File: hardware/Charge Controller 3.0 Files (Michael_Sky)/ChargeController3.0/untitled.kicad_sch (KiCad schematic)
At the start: 3 parts, among them J1 Conn_02x26_Odd_Even, J12 Conn_02x26_Odd_Even, J20 Conn_01x08_Pin

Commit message: fixed merge :(
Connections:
- net 3.3V: now also J12.28 (Pin_28)
- net GND: now also J1.33 (Pin_33), J1.34 (Pin_34), J12.29 (Pin_29), J20.3 (Pin_3), J20.4 (Pin_4)
- net RS SYS2 Tx: now also J1.40 (Pin_40)
- net SYS/BATT: now also J20.1 (Pin_1), J20.2 (Pin_2)
- net UART_RX: now also J1.42 (Pin_42)
- net UART_TX: now also J1.44 (Pin_44)

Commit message: New formatting
New formatting
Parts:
- J20: footprint (none) -> Connector_PinHeader_2.54mm:PinHeader_1x08_P2.54mm_Horizontal
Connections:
- net INT: now also J1.12 (Pin_12); no longer J1.9 (Pin_9)
- net PG: now also J1.10 (Pin_10); no longer J1.18 (Pin_18)
- net SCL: now also J1.18 (Pin_18); no longer J1.10 (Pin_10)
- net SDA: now also J1.16 (Pin_16); no longer J1.12 (Pin_12)
- net STAT_2: now also J1.9 (Pin_9); no longer J1.16 (Pin_16)
- net BATT_PIN: now reaches J12.47 (Pin_47)
- net BATT_PIN: now also J12.45 (Pin_45), J20.1 (Pin_1)
- net SYS_PIN: now reaches J12.48 (Pin_48)
- net SYS_PIN: now also J12.46 (Pin_46), J20.2 (Pin_2)
- net CE: no longer names the net of J1.20 (Pin_20)
- net SOL renamed SOL_PIN
- removed net SYS/BATT: J12.45 (Pin_45), J12.46 (Pin_46), J20.1 (Pin_1), J20.2 (Pin_2)
- no-connect marks 1 -> 69

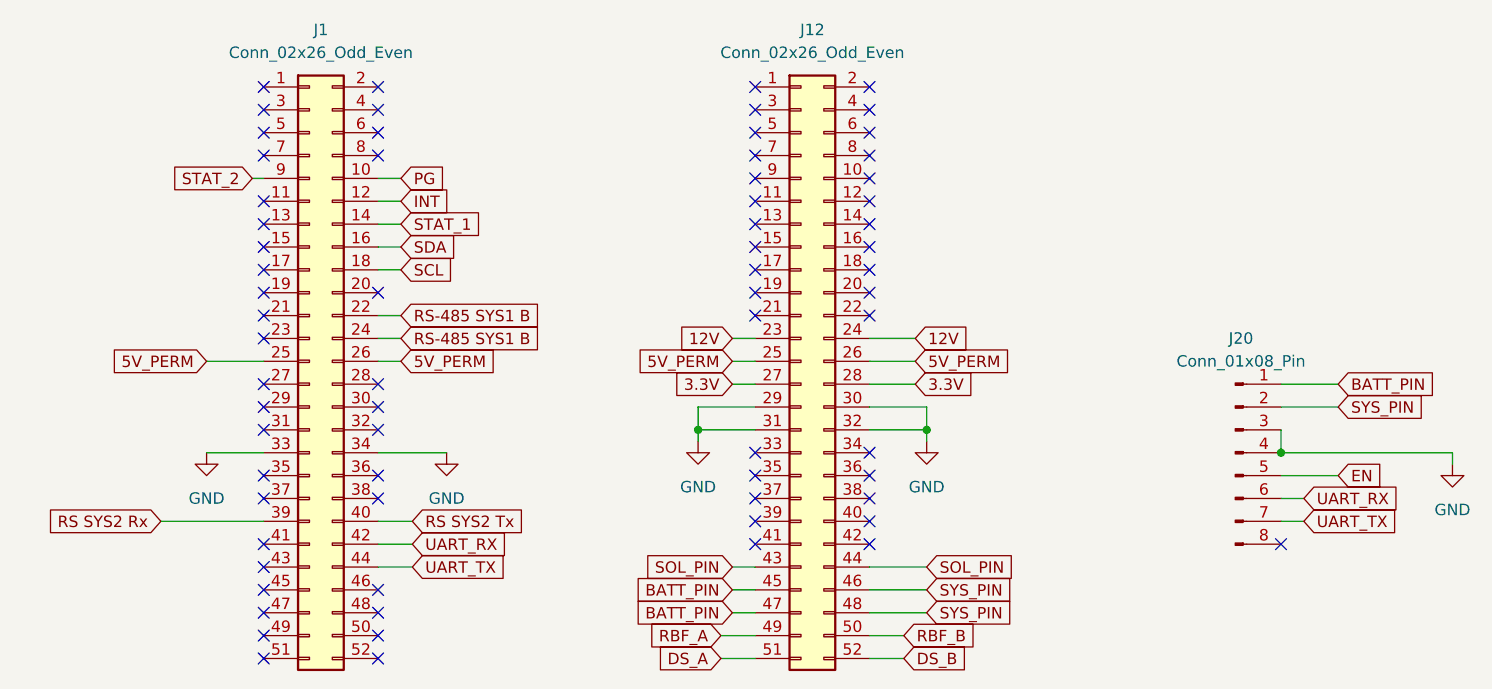
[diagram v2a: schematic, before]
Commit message: Final PCB?
inhibits rework, filtering rework
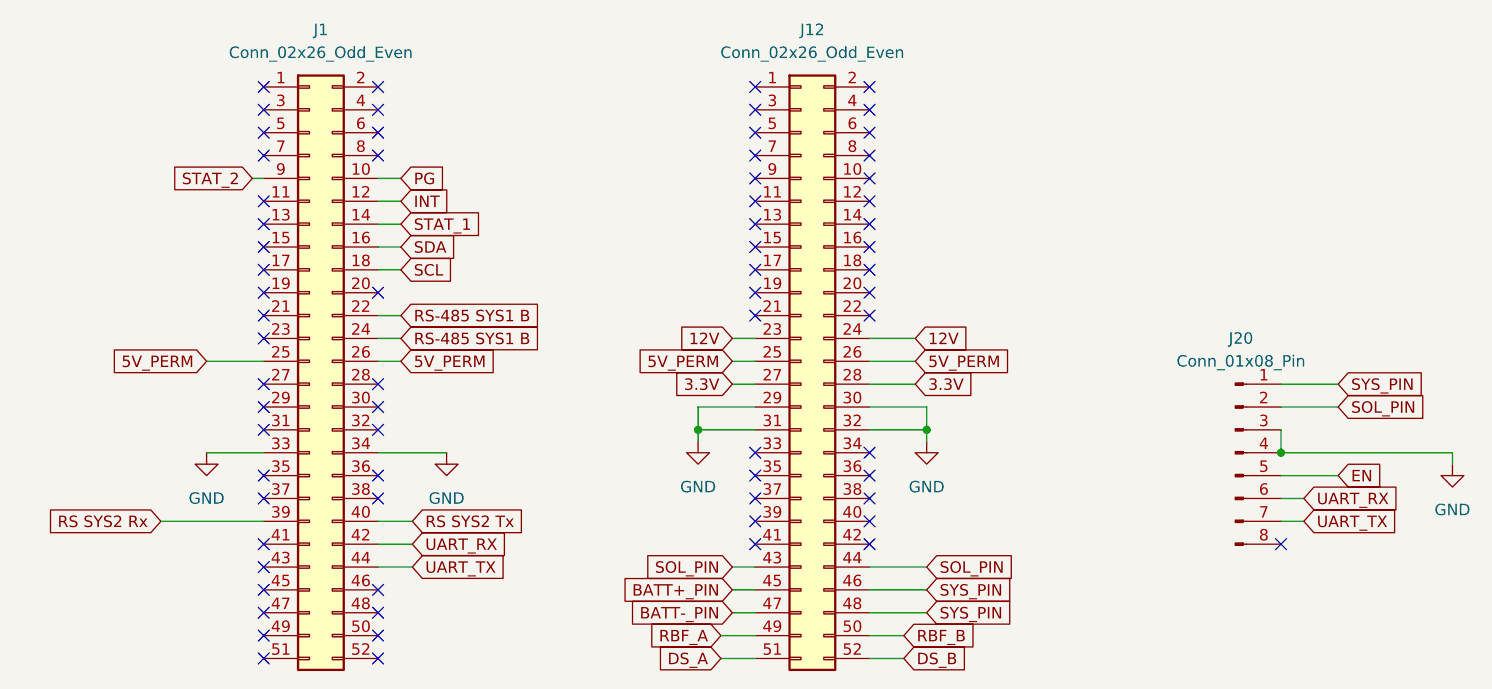
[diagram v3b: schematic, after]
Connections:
- net SOL_PIN: now also J20.2 (Pin_2)
- net SYS_PIN: now also J20.1 (Pin_1); no longer J20.2 (Pin_2)
- removed net BATT_PIN: J12.45 (Pin_45), J12.47 (Pin_47), J20.1 (Pin_1)
- new net BATT+_PIN: J12.45 (Pin_45)
- new net BATT-_PIN: J12.47 (Pin_47)
